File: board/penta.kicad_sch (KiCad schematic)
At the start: 142 parts, among them J1 USB_C_Receptacle_PowerOnly_6P, Q1 SK335N, U1 XIAO-RP2040-SMD

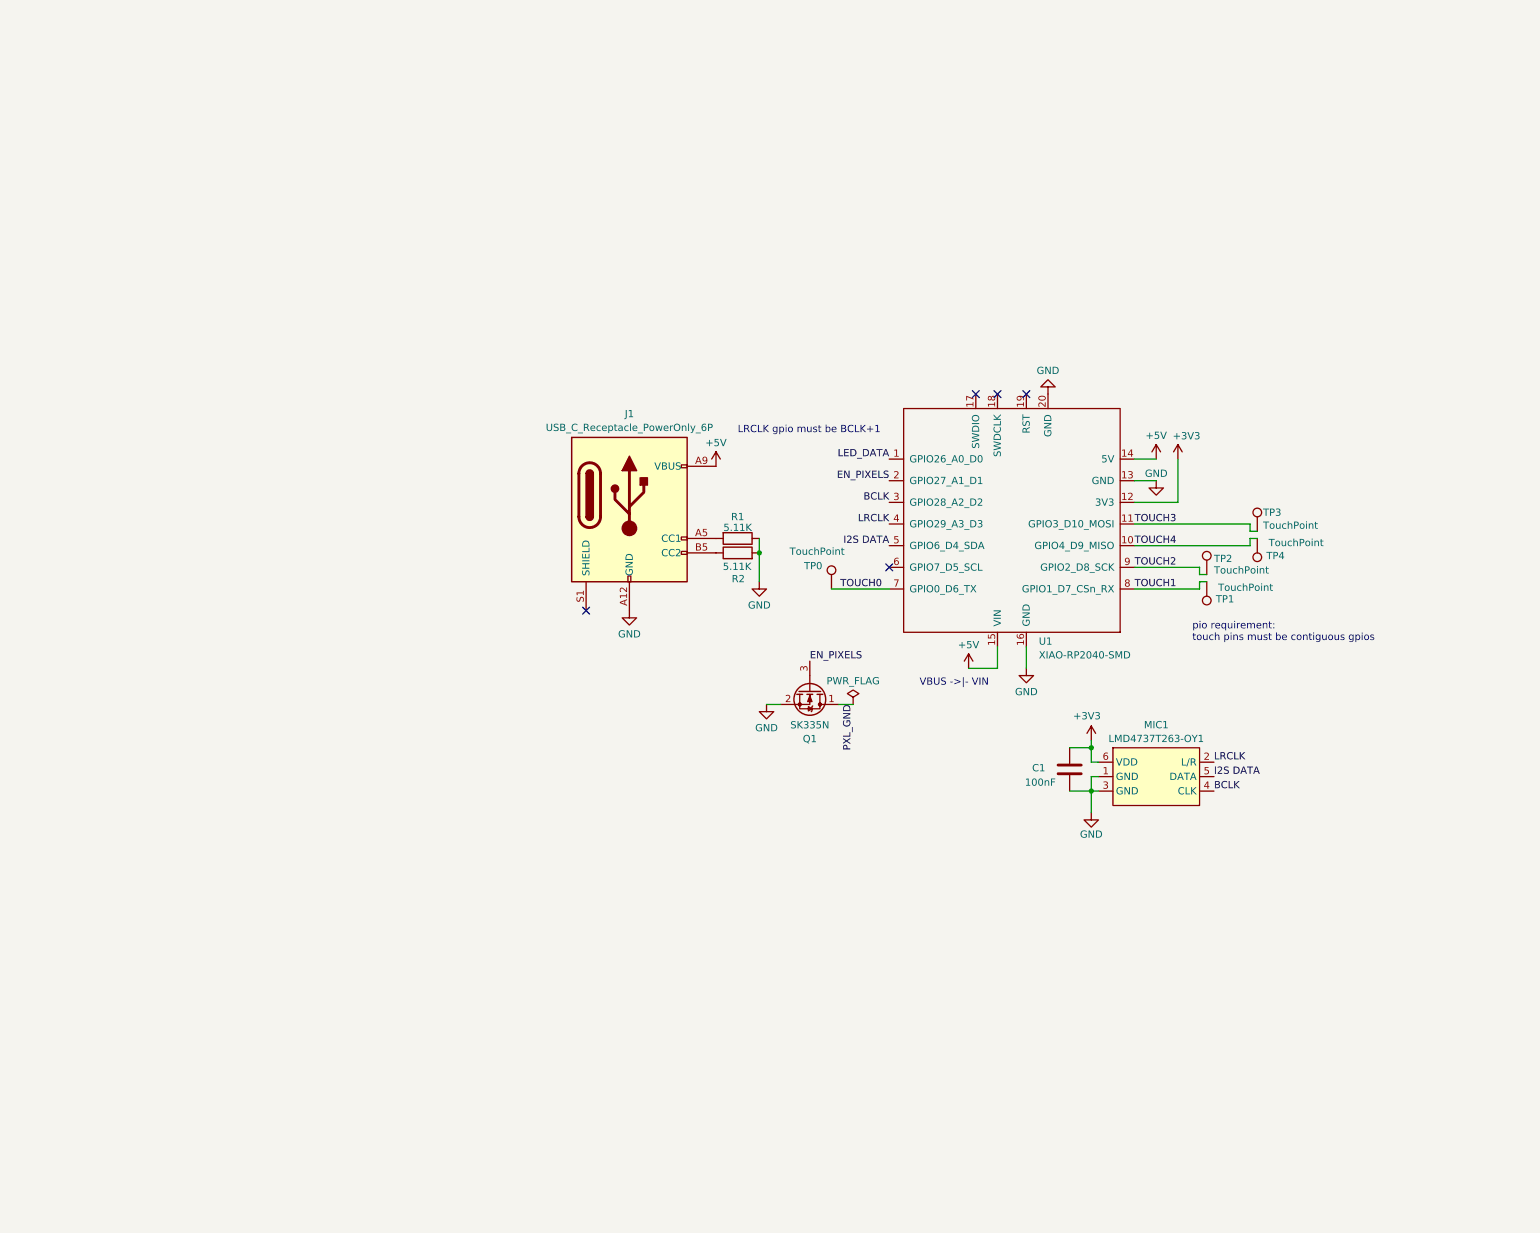
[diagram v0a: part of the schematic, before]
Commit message: drop in an rp2040 and associated circuitry; proper usb port (two of them); bottom-facing mic; do a first pass on layout
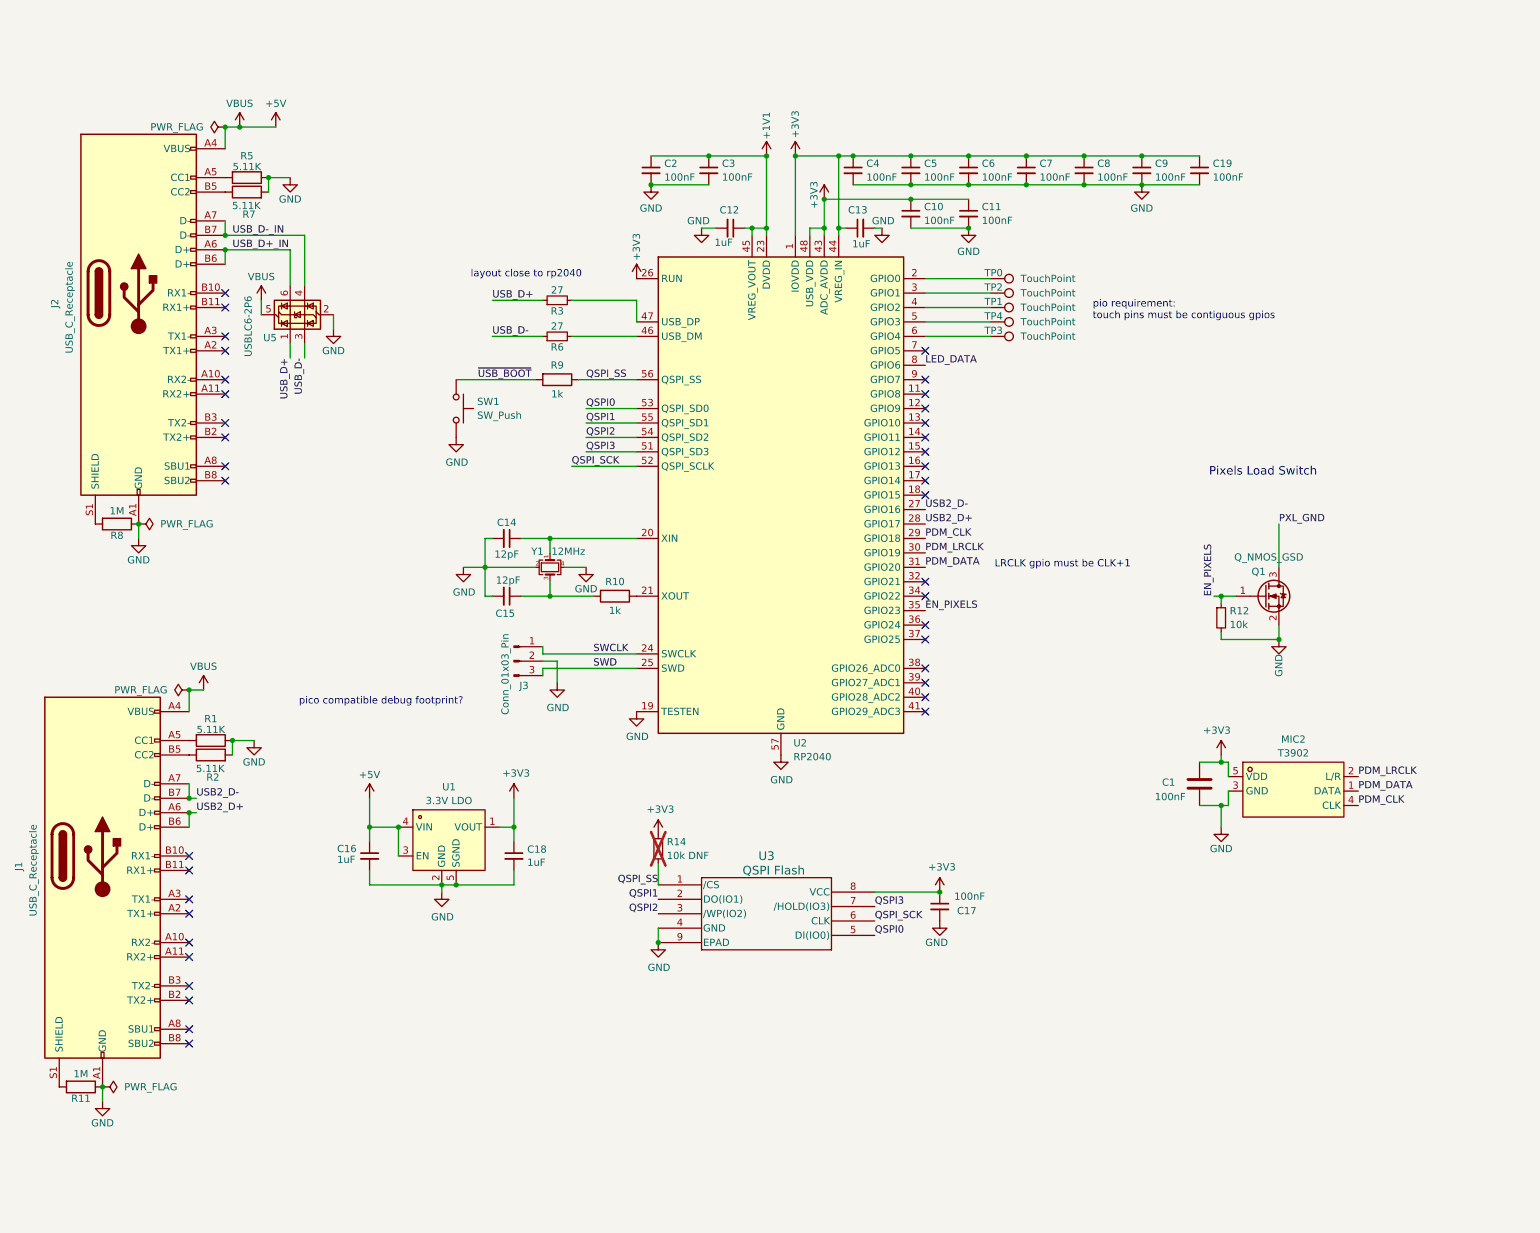
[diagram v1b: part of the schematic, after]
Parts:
- removed J1: USB_C_Receptacle_PowerOnly_6P, penta:USB-C-SMD_TYPE-C-6P-QT073, symbol Connector:USB_C_Receptacle_PowerOnly_6P
- removed MIC1: LMD4737T263-OY1, penta:LGA-6_L4.7-W3.8-P1.65_LMD4737T, symbol penta:LMD4737T263-OY1
- removed Q1: SK335N, Package_TO_SOT_SMD:SOT-23, symbol Device:Q_NMOS_DSG
- removed U1: XIAO-RP2040-SMD, penta:XIAO-RP2040-SMD, symbol penta:XIAO-RP2040-SMD
- added C10, C11, C17, C19, C2, C3, C4, C5, C6, C7, C8, C9: 100nF, Capacitor_SMD:C_0402_1005Metric, symbol Device:C_Small
- added C12, C13, C16, C18: 1uF, Capacitor_SMD:C_0402_1005Metric, symbol Device:C_Small
- added C14, C15: 12pF, Capacitor_SMD:C_0402_1005Metric, symbol Device:C_Small
- added J1, J2: USB_C_Receptacle, penta:USB-SMD_USB-TYPE-C-020, symbol Connector:USB_C_Receptacle
- added J3: Conn_01x03_Pin, Connector_PinSocket_1.27mm:PinSocket_1x03_P1.27mm_Vertical, symbol Connector:Conn_01x03_Pin
- added MIC2: T3902, penta:MIC-SMD_5P-L3.5-W2.7-TL_MMICT390200012, symbol penta:MMICT390200012
- added Q1: Q_NMOS_GSD, Package_TO_SOT_SMD:SOT-23, symbol Device:Q_NMOS_GSD
- added R10, R9: 1k, Resistor_SMD:R_0402_1005Metric, symbol Device:R
- added R11, R8: 1M, Resistor_SMD:R_0402_1005Metric, symbol Device:R
- added R12: 10k, Resistor_SMD:R_0402_1005Metric, symbol Device:R_Small
- added R14: 10k DNF, Resistor_SMD:R_0402_1005Metric, symbol Device:R_Small
- added R3, R6: 27, Resistor_SMD:R_0402_1005Metric, symbol Device:R_Small
- added R5, R7: 5.11K, Resistor_SMD:R_0402_1005Metric, symbol Device:R
- added SW1: SW_Push, penta:KEY-SMD_L3.0-W2.5-LS4.0, symbol Switch:SW_Push
- added U1: 3.3V LDO, Package_DFN_QFN:OnSemi_XDFN4-1EP_1.0x1.0mm_EP0.52x0.52mm, symbol penta:RT9078-33GQZ
- added U2: RP2040, Package_DFN_QFN:QFN-56-1EP_7x7mm_P0.4mm_EP3.2x3.2mm, symbol MCU_RaspberryPi:RP2040
- added U3: QSPI Flash, penta:USON_3X2_WIN, symbol penta:QSPI Flash
- added U5: USBLC6-2P6, Package_TO_SOT_SMD:SOT-666, symbol Power_Protection:USBLC6-2P6
- added Y1: 12MHz, Crystal:Crystal_SMD_2520-4Pin_2.5x2.0mm, symbol Device:Crystal_GND24_Small
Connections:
- net +3V3: now also C10.1, C11.1, C13.1, C17.1, C18.1, C19.1, C4.1, C5.1, C6.1, C7.1, C8.1, C9.1, MIC2.5 (VDD), R14.1, U1.1 (VOUT), U2.1 (IOVDD), U2.10 (IOVDD), U2.22 (IOVDD), U2.26 (RUN), U2.33 (IOVDD), U2.42 (IOVDD), U2.43 (ADC_AVDD), U2.44 (VREG_IN), U2.48 (USB_VDD), U2.49 (IOVDD), U3.8 (VCC)
- net +5V: now also C16.1, J1.A4 (VBUS), J1.A9 (VBUS), J1.B4 (VBUS), J1.B9 (VBUS), J2.A4 (VBUS), J2.A9 (VBUS), J2.B4 (VBUS), J2.B9 (VBUS), U1.3 (EN), U1.4 (VIN), U5.5 (VBUS)
- net EN_PIXELS: now also Q1.1 (G), R12.1, U2.35 (GPIO23)
- net GND: now also C10.2, C11.2, C12.2, C13.2, C14.2, C15.2, C16.2, C17.2, C18.2, C19.2, C2.2, C3.2, C4.2, C5.2, C6.2, C7.2, C8.2, C9.2, J1.A1 (GND), J1.A12 (GND), J1.B1 (GND), J1.B12 (GND), J2.A1 (GND), J2.A12 (GND), J2.B1 (GND), J2.B12 (GND), J3.2 (Pin_2), MIC2.3 (GND), Q1.2 (S), R11.1, R12.2, R5.1, R7.2, R8.1, SW1.2, U1.2 (GND), U1.5 (SGND), U2.19 (TESTEN), U2.57 (GND), U3.4 (GND), U3.9 (EPAD), U5.2 (GND), Y1.2, Y1.4
- net LED_DATA: now also U2.8 (GPIO6)
- net PXL_GND: now also Q1.3 (D)
- net at R2.1: now also J1.B5 (CC2)
- net at R1.2: now also J1.A5 (CC1)
- net TOUCH0: no longer names the net of TP0.1
- net TOUCH0: now also U2.2 (GPIO0)
- net TOUCH1: no longer names the net of TP1.1
- net TOUCH1: now also U2.4 (GPIO2)
- net TOUCH2: no longer names the net of TP2.1
- net TOUCH2: now also U2.3 (GPIO1)
- net TOUCH3: no longer names the net of TP3.1
- net TOUCH3: now also U2.6 (GPIO4)
- net TOUCH4: no longer names the net of TP4.1
- net TOUCH4: now also U2.5 (GPIO3)
- new net: R10.1, U2.21 (XOUT)
- new net: C15.1, R10.2, Y1.3
- new net: J2.A5 (CC1), R5.2
- new net: J2.B5 (CC2), R7.1
- new net: J2.S1 (SHIELD), R8.2
- new net: R6.2, U2.46 (USB_DM)
- new net: C14.1, U2.20 (XIN), Y1.1
- new net: R3.2, U2.47 (USB_DP)
- new net: J1.S1 (SHIELD), R11.2
- new net +1V1: C12.1, C2.1, C3.1, U2.23 (DVDD), U2.45 (VREG_VOUT), U2.50 (DVDD)
- new net PDM_CLK: MIC2.4 (CLK), U2.29 (GPIO18)
- new net PDM_DATA: MIC2.1 (DATA), U2.31 (GPIO20)
- new net PDM_LRCLK: MIC2.2 (L/R), U2.30 (GPIO19)
- new net QSPI0: U2.53 (QSPI_SD0), U3.5 (DI(IO0))
- new net QSPI1: U2.55 (QSPI_SD1), U3.2 (DO(IO1))
- new net QSPI2: U2.54 (QSPI_SD2), U3.3 (/WP(IO2))
- new net QSPI3: U2.51 (QSPI_SD3), U3.7 (/HOLD(IO3))
- new net QSPI_SCK: U2.52 (QSPI_SCLK), U3.6 (CLK)
- new net QSPI_SS: R14.2, R9.1, U2.56 (QSPI_SS), U3.1 (/CS)
- new net SWCLK: J3.1 (Pin_1), U2.24 (SWCLK)
- new net SWD: J3.3 (Pin_3), U2.25 (SWD)
- new net USB2_D+: J1.A6 (D+), J1.B6 (D+), U2.28 (GPIO17)
- new net USB2_D-: J1.A7 (D-), J1.B7 (D-), U2.27 (GPIO16)
- new net USB_D+: R3.1, U5.1 (I/O1)
- new net USB_D+_IN: J2.A6 (D+), J2.B6 (D+), U5.6 (I/O1)
- new net USB_D-: R6.1, U5.3 (I/O2)
- new net USB_D-_IN: J2.A7 (D-), J2.B7 (D-), U5.4 (I/O2)
- new net ~{USB_BOOT}: R9.2, SW1.1
- no-connect marks 6 -> 39
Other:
- note added: "LRCLK gpio must be CLK+1"
- note added: "Pixels Load Switch"
- note added: "layout close to rp2040"
- note added: "pico compatible debug footprint?"
- note removed: "LRCLK gpio must be BCLK+1"
- note removed: "VBUS ->|- VIN"
- moved on the sheet: C1

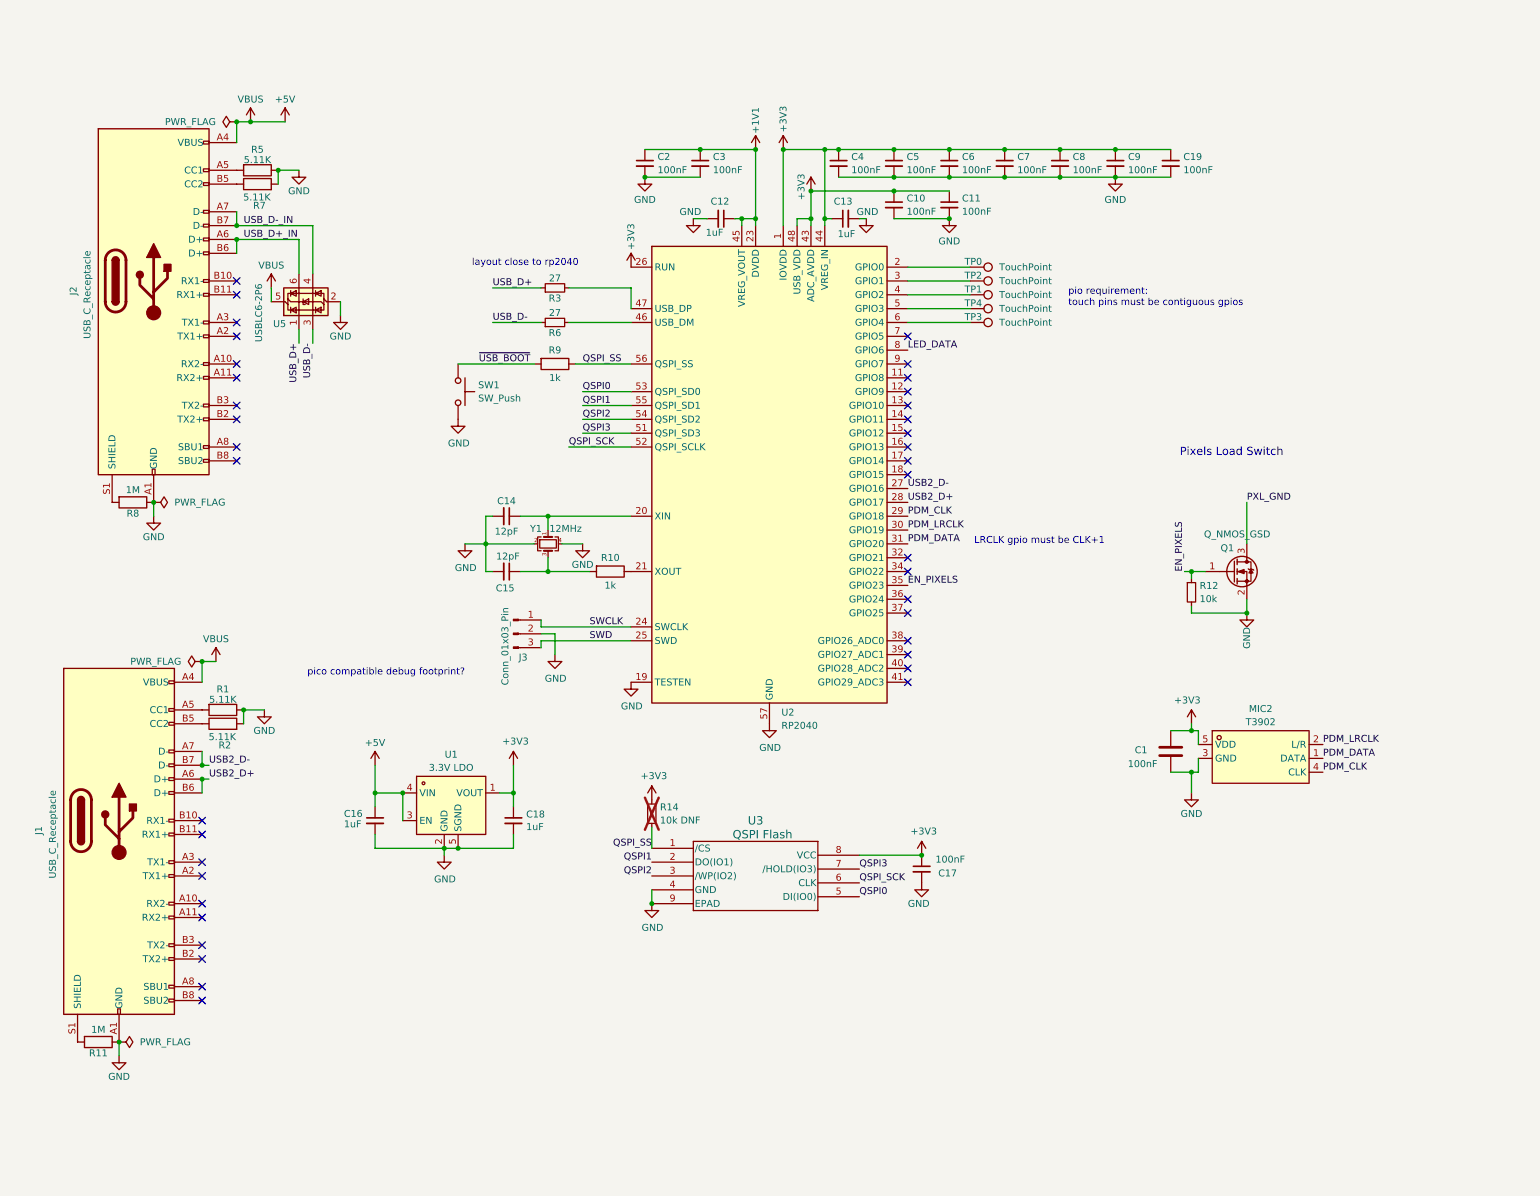
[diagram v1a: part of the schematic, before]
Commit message: add a usb mux for communicating between pentas and make a draft layout
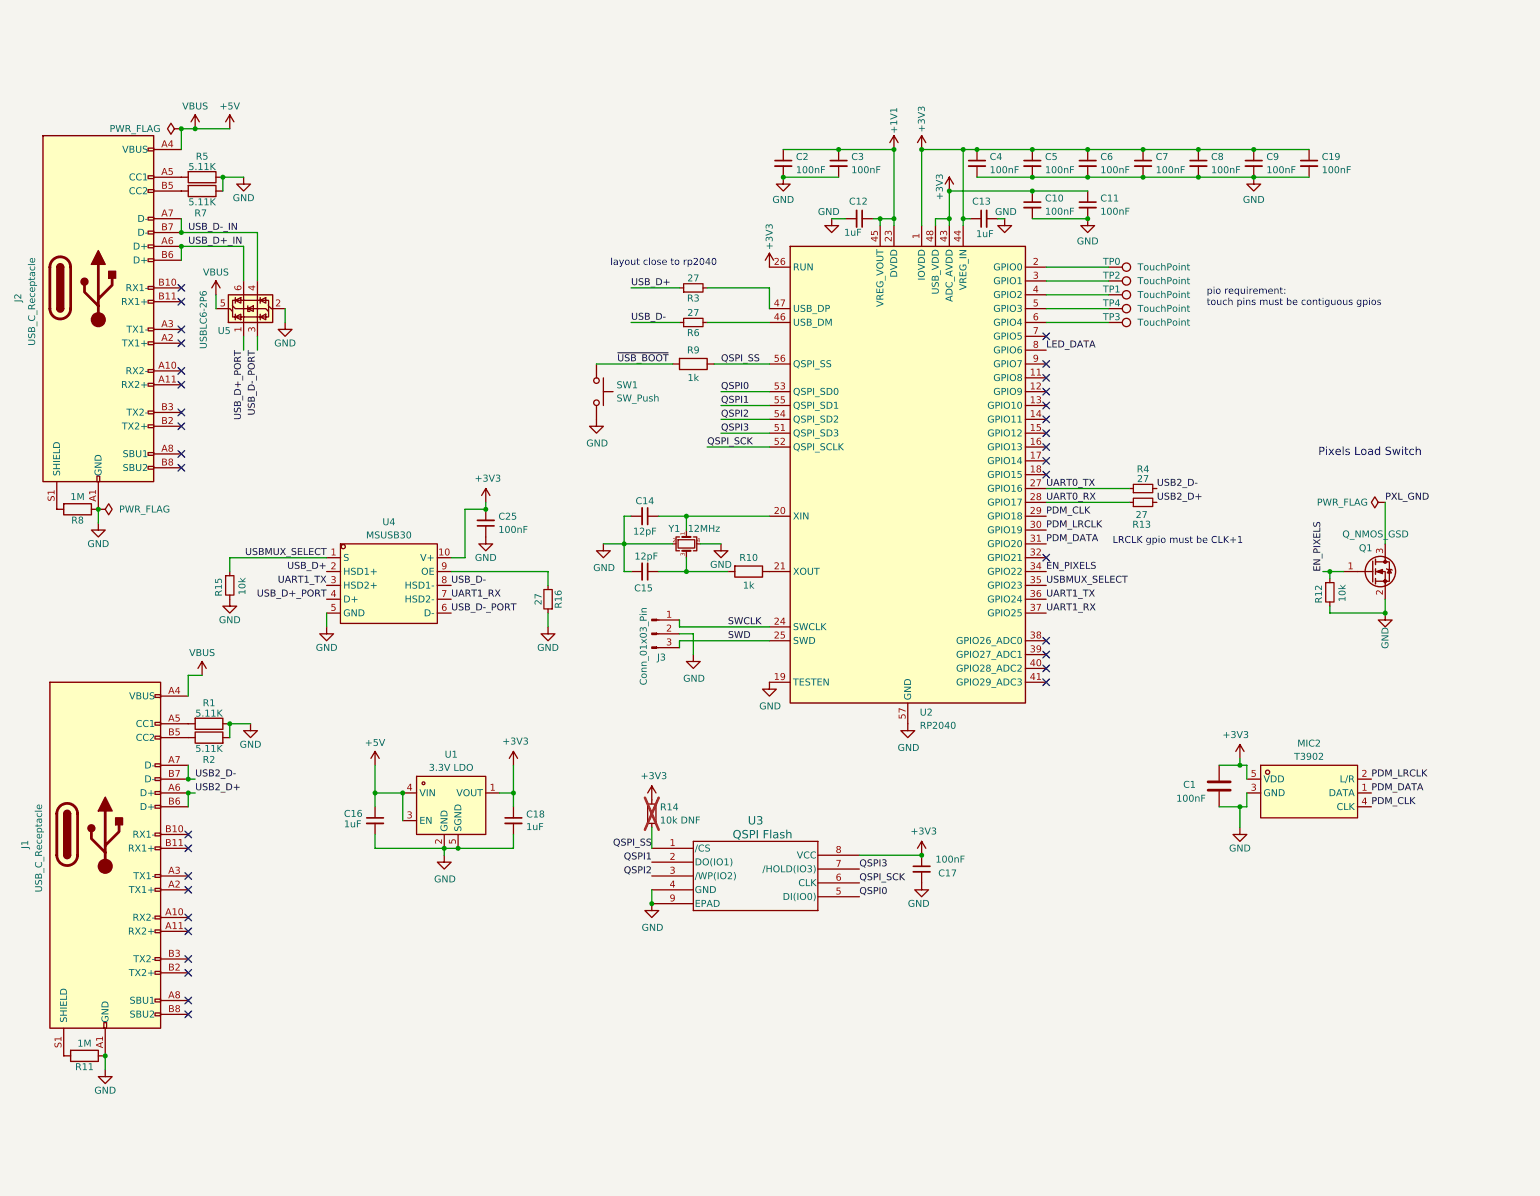
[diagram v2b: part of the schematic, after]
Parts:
- added C25: 100nF, Capacitor_SMD:C_0402_1005Metric, symbol Device:C_Small
- added R13, R16, R4: 27, Resistor_SMD:R_0402_1005Metric, symbol Device:R_Small
- added R15: 10k, Resistor_SMD:R_0402_1005Metric, symbol Device:R_Small
- added U4: MSUSB30, Package_SO:MSOP-10_3x3mm_P0.5mm, symbol penta:MSUSB30
- J3: footprint Connector_PinSocket_1.27mm:PinSocket_1x03_P1.27mm_Vertical -> penta:SMD_Pad_01x03_1.27mm
- R1, R2, R5, R7: Designation RC0402FR-07511KL -> RC0402FR-075K11L; LCSC C163461 -> C274895
- R12: Designation (none) -> RC0402FR-0710KL; LCSC (none) -> C60490
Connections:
- net +3V3: now also C25.2, U4.10 (V+)
- net EN_PIXELS: now also U2.34 (GPIO22); no longer U2.35 (GPIO23)
- net GND: now also R7.1, C25.1, R15.2, R16.1, U4.5 (GND); no longer R7.2
- net USB2_D+: now also R13.2; no longer U2.28 (GPIO17)
- net USB2_D-: now also R4.2; no longer U2.27 (GPIO16)
- net USB_D+: now also U4.2 (HSD1+); no longer U5.1 (I/O1)
- net USB_D-: now also U4.8 (HSD1-); no longer U5.3 (I/O2)
- net at J2.B5 (CC2): now also R7.2; no longer R7.1
- net UART1_TX: now reaches U2.36 (GPIO24)
- net UART1_TX: now also U4.3 (HSD2+)
- net UART1_RX: now reaches U2.37 (GPIO25)
- net UART1_RX: now also U4.7 (HSD2-)
- new net: R16.2, U4.9 (OE)
- new net UART0_RX: R13.1, U2.28 (GPIO17)
- new net UART0_TX: R4.1, U2.27 (GPIO16)
- new net USBMUX_SELECT: R15.1, U2.35 (GPIO23), U4.1 (S)
- new net USB_D+_PORT: U4.4 (D+), U5.1 (I/O1)
- new net USB_D-_PORT: U4.6 (D-), U5.3 (I/O2)
- no-connect marks 39 -> 36
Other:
- note removed: "pico compatible debug footprint?"
- moved on the sheet: C1, C10, C11, C12, C13, C14, C15, C19, C2, C3, C4, C5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

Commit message: polish & readiness
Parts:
- added TP5: TestPoint, TestPoint:TestPoint_Pad_D1.0mm, symbol Connector:TestPoint
- MIC2: footprint penta:MIC-SMD_5P-L3.5-W2.7-TL_MMICT390200012 -> penta:MIC_T3902
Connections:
- net at U2.38 (GPIO26_ADC0): now also TP5.1
- no-connect marks 36 -> 35
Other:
- moved on the sheet: C25, R15, R16, U4
